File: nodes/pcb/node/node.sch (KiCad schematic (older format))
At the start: 33 parts, among them J1 Top Hemisphere, J2 FTDI Basic, J3 Burner, J4 Port, J5 Port, J6 Bottom Hemisphere, J7 Port, J8 Port, U1 MIC5205YM5, U2 ATmega328P-AU, U3 LP2985-3.3, U4 ADXL335, Y1 16MHz

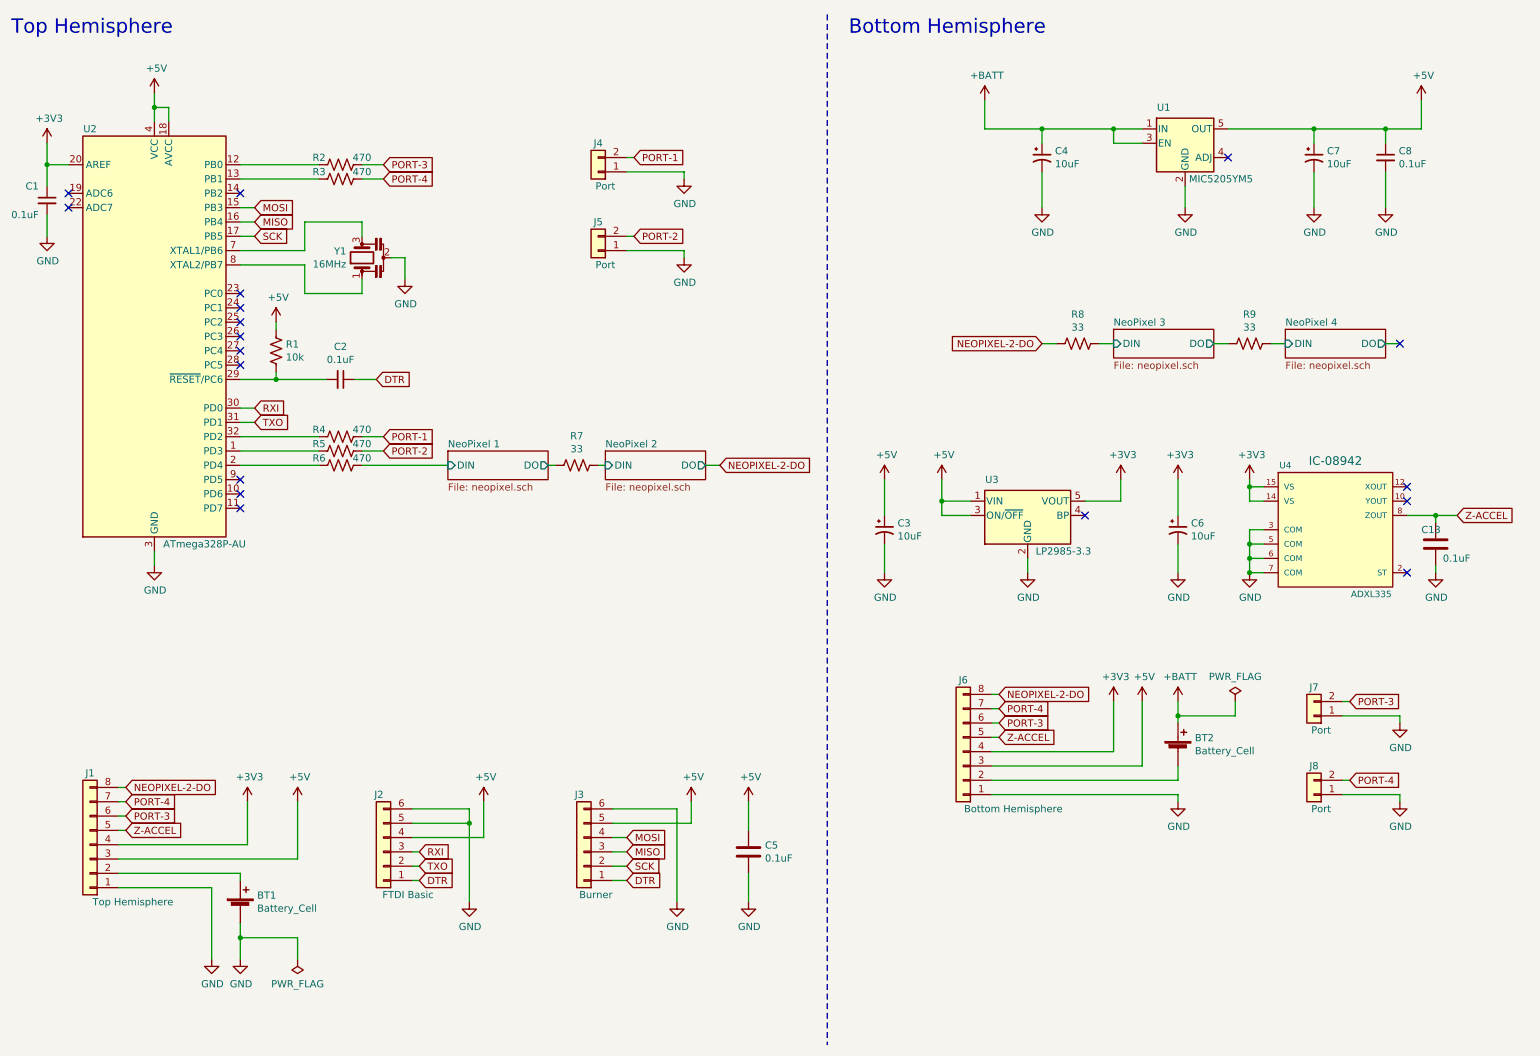
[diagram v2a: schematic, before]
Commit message: Start simplified Seeed OPL compatible circuit
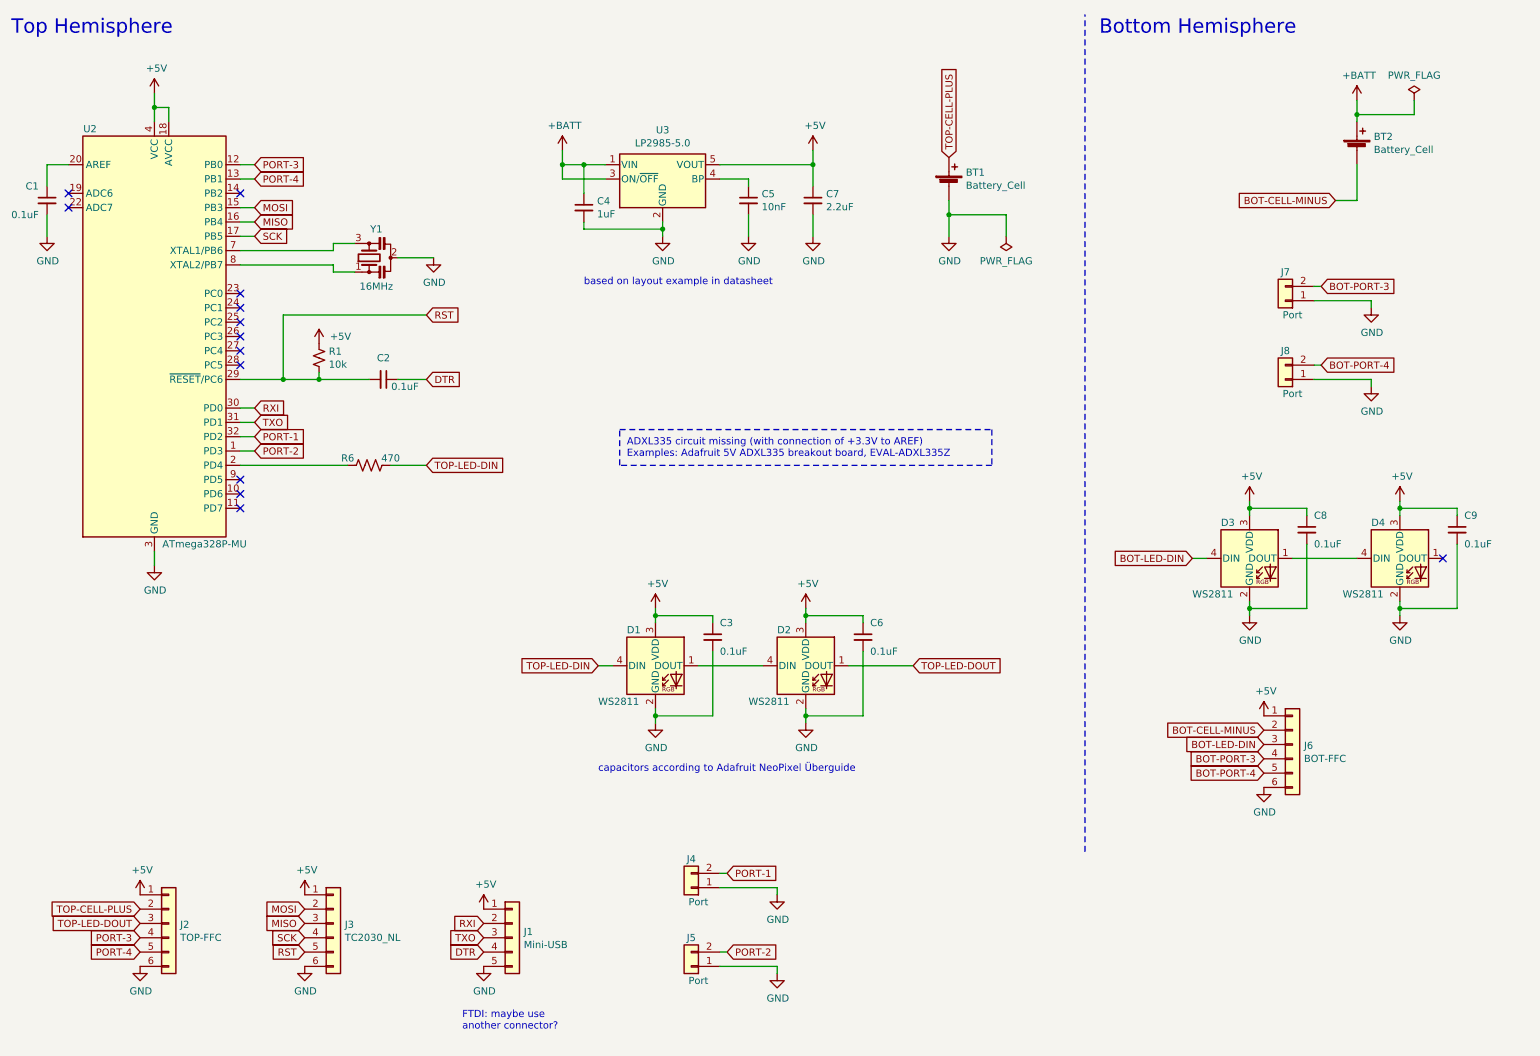
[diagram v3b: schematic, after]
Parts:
- removed C13, C5: 0.1uF, Capacitor_SMD:C_0603_1608Metric_Pad1.05x0.95mm_HandSolder, symbol Device:C
- removed C3, C4, C6, C7: 10uF, Capacitor_Tantalum_SMD:CP_EIA-3216-18_Kemet-A_Pad1.58x1.35mm_HandSolder, symbol Device:CP1_Small
- removed J1: Top Hemisphere, Connector_PinHeader_2.54mm:PinHeader_2x04_P2.54mm_Vertical, symbol Connector_Generic:Conn_01x08
- removed J6: Bottom Hemisphere, Connector_PinHeader_2.54mm:PinHeader_2x04_P2.54mm_Vertical, symbol Connector_Generic:Conn_01x08
- removed R1: 10k, Resistor_SMD:R_0603_1608Metric_Pad1.05x0.95mm_HandSolder, symbol Device:R_US
- removed R2, R3, R4, R5: 470, Resistor_SMD:R_0603_1608Metric_Pad1.05x0.95mm_HandSolder, symbol Device:R_US
- removed R7, R8, R9: 33, Resistor_SMD:R_0603_1608Metric_Pad1.05x0.95mm_HandSolder, symbol Device:R_US
- removed U1: MIC5205YM5, Package_TO_SOT_SMD:SOT-23-5, symbol Regulator_Linear:MIC5205YM5
- removed U3: LP2985-3.3, Package_TO_SOT_SMD:SOT-23-5, symbol Regulator_Linear:LP2985-3.3
- removed U4: ADXL335, Package_CSP:LFCSP-16-1EP_4x4mm_P0.65mm_EP2.1x2.1mm, symbol SparkFun-Sensors:ADXL335
- removed Y1: 16MHz, Crystal:Resonator_SMD_muRata_CSTxExxV-3Pin_3.0x1.1mm_HandSoldering, symbol Device:Resonator
- added C3, C6, C9: 0.1uF, Capacitor_SMD:C_0402_1005Metric, symbol Device:C_Small
- added C4: 1uF, Capacitor_SMD:C_0402_1005Metric, symbol Device:C_Small
- added C5: 10nF, Capacitor_SMD:C_0402_1005Metric, symbol Device:C_Small
- added C7: 2.2uF, Capacitor_SMD:C_0402_1005Metric, symbol Device:C_Small
- added D1, D2, D3, D4: WS2811, Connector_PinHeader_1.27mm:PinHeader_1x04_P1.27mm_Vertical, symbol LED:NeoPixel_THT
- added J1: Mini-USB, Connector_USB:USB_Mini-B_Lumberg_2486_01_Horizontal, symbol Connector_Generic:Conn_01x05
- added J6: BOT-FFC, Connector_FFC-FPC:Hirose_FH12-6S-0.5SH_1x06-1MP_P0.50mm_Horizontal, symbol Connector_Generic:Conn_01x06
- added R1: 10k, Resistor_SMD:R_0402_1005Metric, symbol Device:R_Small_US
- added U3: LP2985-5.0, Package_TO_SOT_SMD:SOT-23-5, symbol Regulator_Linear:LP2985-5.0
- added Y1: 16MHz, Crystal:Resonator_SMD_muRata_CSTxExxV-3Pin_3.0x1.1mm, symbol Device:Resonator_Small
- C1, C2, C8: footprint Capacitor_SMD:C_0603_1608Metric_Pad1.05x0.95mm_HandSolder -> Capacitor_SMD:C_0402_1005Metric
- J2: value FTDI Basic -> TOP-FFC; footprint Common-Parts-Library:HARWIN_M20-7910642R -> Connector_FFC-FPC:Hirose_FH12-6S-0.5SH_1x06-1MP_P0.50mm_Horizontal
- J3: value Burner -> TC2030_NL; footprint Connector_PinSocket_2.54mm:PinSocket_1x06_P2.54mm_Vertical -> Connector:Tag-Connect_TC2030-IDC-NL_2x03_P1.27mm_Vertical
- U2: value ATmega328P-AU -> ATmega328P-MU; footprint Package_QFP:TQFP-32_7x7mm_P0.8mm -> Package_DFN_QFN:VQFN-32-1EP_5x5mm_P0.5mm_EP3.1x3.1mm
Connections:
- net +5V: now also J2.1 (Pin_1), J3.1 (Pin_1), C3.1, C6.1, C7.1, C9.1, D1.3 (VDD), D2.3 (VDD), D3.3 (VDD), D4.3 (VDD), J1.1 (Pin_1), J6.1 (Pin_1), R1.1, U3.5 (VOUT); no longer J2.4 (Pin_4), J3.5 (Pin_5)
- net +BATT: now also C4.1, U3.1 (VIN), U3.3 (ON/~OFF~)
- net DTR: now also J1.4 (Pin_4); no longer J2.1 (Pin_1), J3.1 (Pin_1)
- net GND: now also C3.2, C4.2, C5.2, C6.2, C7.2, C9.2, D1.2 (GND), D2.2 (GND), D3.2 (GND), D4.2 (GND), J1.5 (Pin_5), J6.6 (Pin_6), U3.2 (GND), Y1.2; no longer J2.5 (Pin_5)
- net MOSI: now also J3.2 (Pin_2); no longer J3.4 (Pin_4)
- net PORT-1: now also U2.32 (PD2)
- net PORT-2: now also U2.1 (PD3)
- net PORT-3: now also J2.4 (Pin_4), U2.12 (PB0); no longer J7.2 (Pin_2)
- net PORT-4: now also J2.5 (Pin_5), U2.13 (PB1); no longer J8.2 (Pin_2)
- net RXI: now also J1.2 (Pin_2); no longer J2.3 (Pin_3)
- net SCK: now also J3.4 (Pin_4); no longer J3.2 (Pin_2)
- net TXO: now also J1.3 (Pin_3); no longer J2.2 (Pin_2)
- net at U2.8 (XTAL2/PB7): now also Y1.1
- net at U2.7 (XTAL1/PB6): now also Y1.3
- net RST: now reaches C2.2, U2.29 (~RESET~/PC6)
- net RST: now also J3.5 (Pin_5), R1.2
- net TOP-CELL-PLUS: now reaches BT1.1 (+)
- net TOP-CELL-PLUS: now also J2.2 (Pin_2)
- net BOT-CELL-MINUS: now reaches BT2.2 (-)
- net BOT-CELL-MINUS: now also J6.2 (Pin_2)
- net +3V3: no longer names the net of C1.1, U2.20 (AREF)
- net NeoPixel 1/DIN renamed TOP-LED-DIN
- net TOP-LED-DIN: now also D1.4 (DIN)
- new net: D1.1 (DOUT), D2.4 (DIN)
- new net: C5.1, U3.4 (BP)
- new net: D3.1 (DOUT), D4.4 (DIN)
- new net BOT-LED-DIN: D3.4 (DIN), J6.3 (Pin_3)
- new net BOT-PORT-3: J6.4 (Pin_4), J7.2 (Pin_2)
- new net BOT-PORT-4: J6.5 (Pin_5), J8.2 (Pin_2)
- new net TOP-LED-DOUT: D2.1 (DOUT), J2.3 (Pin_3)
- no-connect marks 18 -> 13
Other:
- note added: "ADXL335 circuit missing (with connection of +3.3V to AREF)\nExamples: Adafruit 5V ADXL335 breakout board, EVAL-ADXL335Z"
- note added: "FTDI: maybe use\nanother connector?"
- note added: "based on layout example in datasheet"
- note added: "capacitors according to Adafruit NeoPixel Überguide"
- moved on the sheet: BT1, BT2, C2, J4, J5, J7, J8, R6
